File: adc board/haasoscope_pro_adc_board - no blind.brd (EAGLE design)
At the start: 157 x 110 mm, 164 parts, among them IC1 ADC12DL2500ACF, IC2 SN74AVC4T774PWR, J1 8pin, J10 8pin, J11 8pin, J12 8pin, J13 8pin, J16 8pin, J17 8pin, J2 8pin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

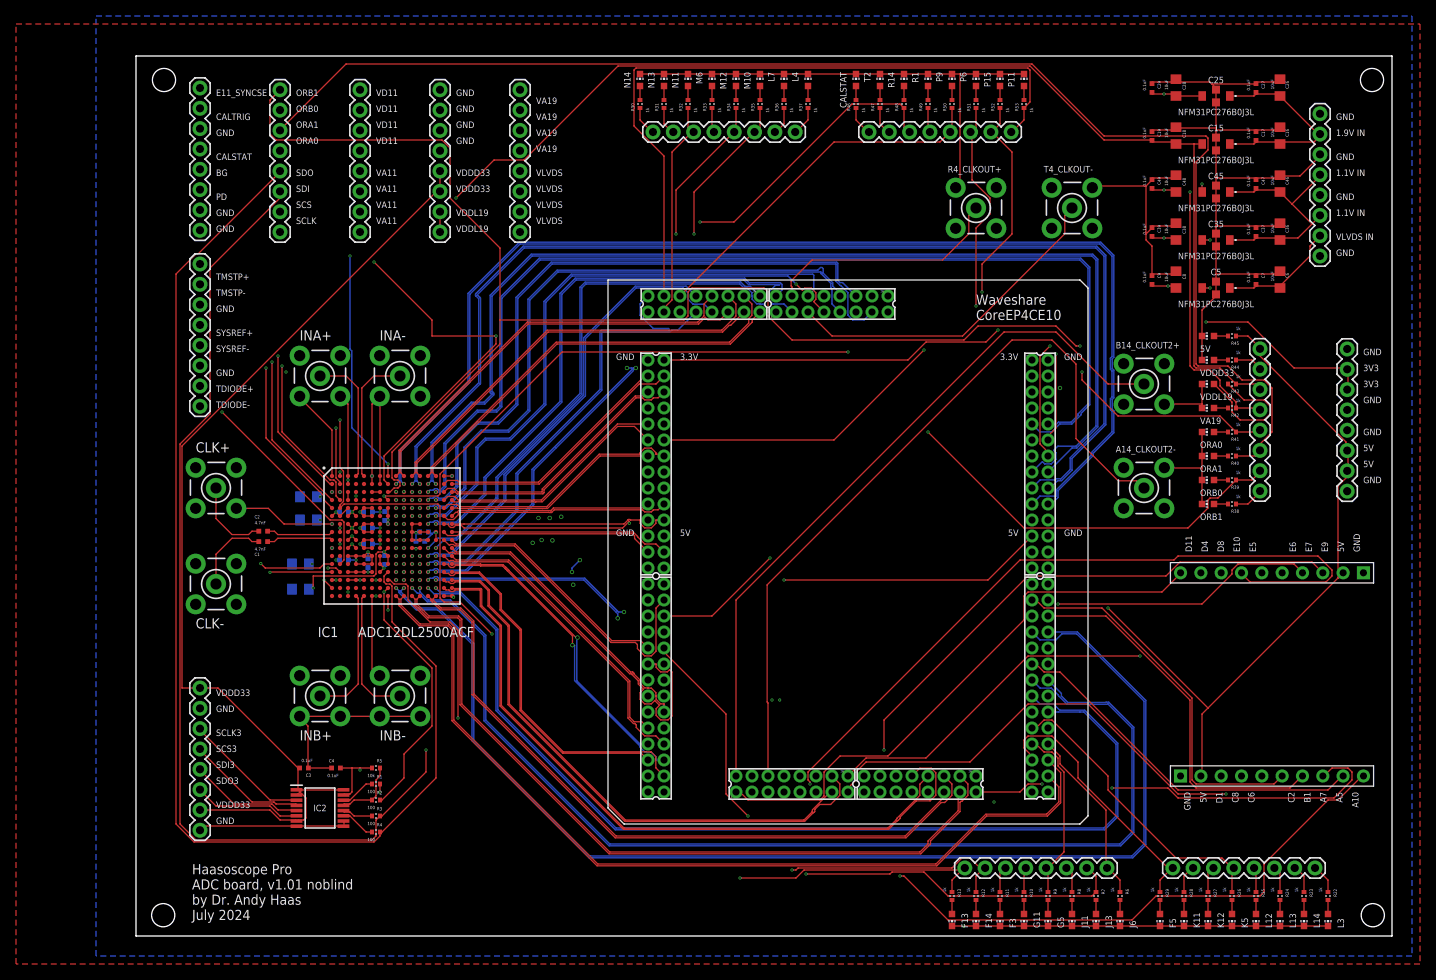
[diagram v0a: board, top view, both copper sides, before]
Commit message: fix pins for bottom rows of fpga
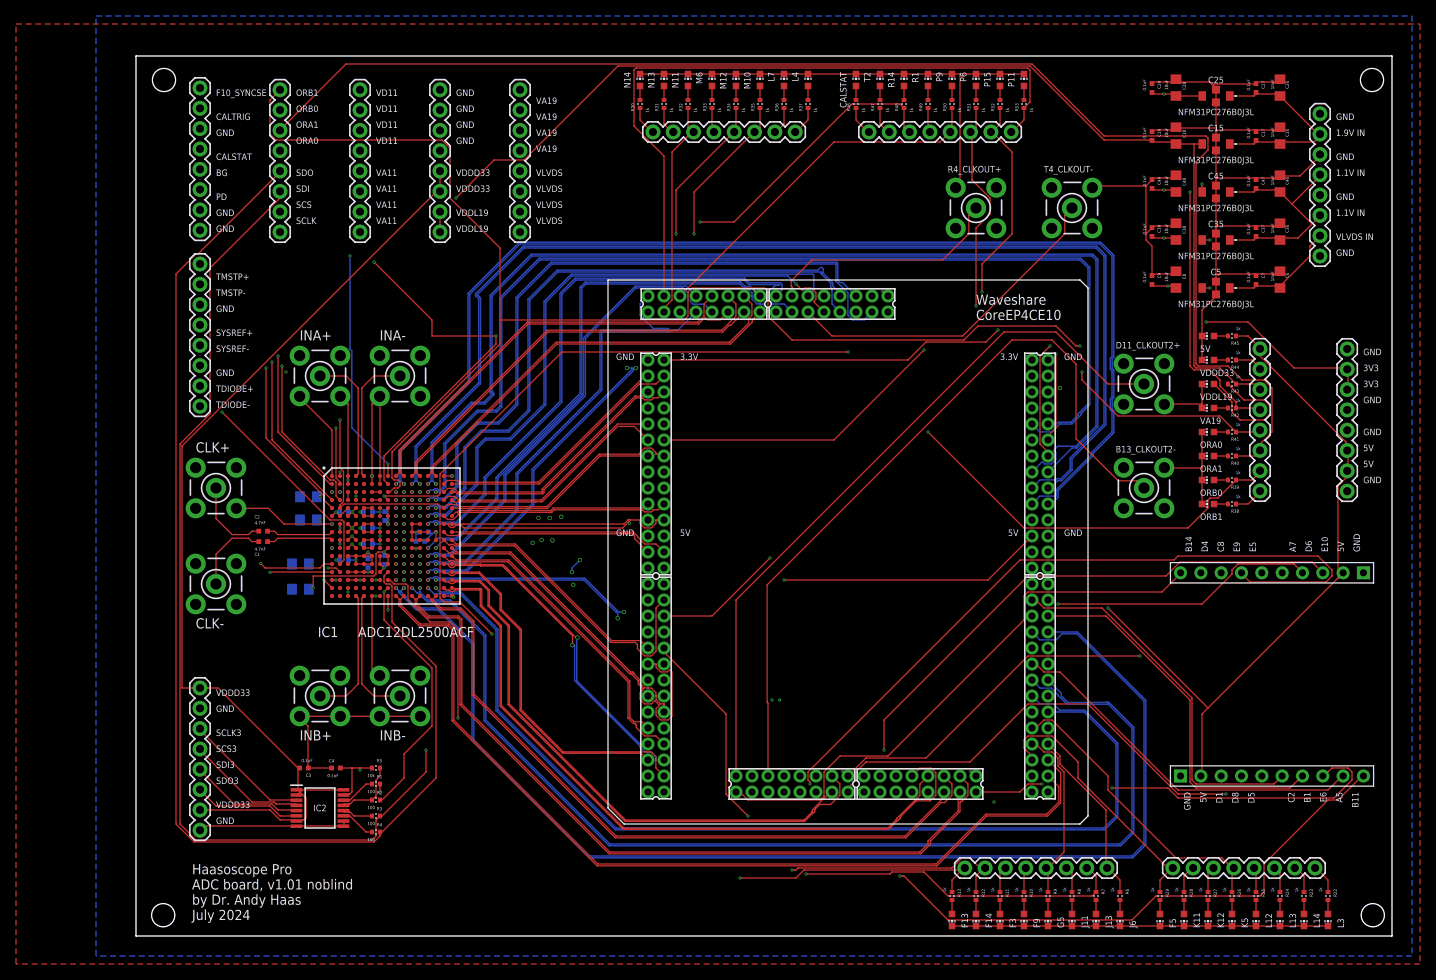
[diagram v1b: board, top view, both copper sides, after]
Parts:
- renumbered A14_CLKOUT2- to B13_CLKOUT2-, B14_CLKOUT2+ to D11_CLKOUT2+
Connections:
- net A10 renamed B11
- net A14_CLKOUT2N renamed B13_CLKOUT2N
- net B14_CLKOUT2P renamed D11_CLKOUT2P
- net C6 renamed D5
- net D11 renamed B14
- net E11_SYNCSE renamed F10_SYNCSE
- net E7 renamed D6
- net G11 renamed F9
- net A7: now also PINOUT2.5, X2.15; no longer PINOUT1.8, X2.16
- net C8: now also PINOUT2.8, X1.16; no longer PINOUT1.4, X1.15
- net D8: now also PINOUT1.4, X1.15; no longer PINOUT2.8, X1.16
- net E10: now also PINOUT2.3, X2.2; no longer PINOUT2.7, X2.1
- net E6: now also PINOUT1.8, X2.16; no longer PINOUT2.5, X2.15
- net E9: now also PINOUT2.7, X2.1; no longer PINOUT2.3, X2.2
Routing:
- net E9: track 71.6 -> 99.1 mm
- net E10: track 99.1 -> 71.6 mm
- net E6: track 49.7 -> 56.0 mm
- net A7: track 56.0 -> 49.7 mm
- net D8: track 57.4 -> 60.5 mm
- net C8: track 60.5 -> 57.4 mm
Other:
- board text added: "B11"
- board text added: "B14"
- board text added: "D5"
- board text added: "D6"
- board text added: "F10_SYNCSE"
- board text added: "F9"
- board text removed: "A10"
- board text removed: "C6"
- board text removed: "D11"
- board text removed: "E11_SYNCSE"
- board text removed: "E7"
- board text removed: "G11"
